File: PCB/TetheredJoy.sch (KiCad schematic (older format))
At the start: 9 parts

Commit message: worked on schematic
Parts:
- added D? (x4): LED, symbol Device:LED
- added R? (x5): 470, symbol Device:R_Small
- added R? (x5): 47K, symbol Device:R_Small
- added SW? (x4): SW_Push, symbol Switch:SW_Push
- R?: value R_Small -> 470
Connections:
- net +5V: now also C?.1, C?.1, J?.2 (Pin_2), U?.14 (VDD), R?.1, R?.1, R?.1, R?.1, R?.1, R?.1, R?.1, R?.1, R?.1
- net GND: now also C?.2, J?.3 (Pin_3), U?.5 (VSS), SW?.2, SW?.2, SW?.2, SW?.2
- net at U?.1 (Vref/AN2/RA2): now also J?.5 (Pin_5), R?.2
- net LED4SW4: now reaches U?.10 (RB4/PGM)
- net LED4SW4: now also D?.1 (K), R?.2, SW?.1
- net TX: now reaches U?.11 (RB5)
- net TX: now also J?.4 (Pin_4)
- net PGC: now reaches U?.12 (RB6/T1OSC0/T1CKI/PGC)
- net PGC: now also J?.5 (Pin_5)
- net PGD: now reaches U?.13 (RB7/T1OSI/PGD)
- net PGD: now also J?.4 (Pin_4)
- net at U?.15 (CLKOUT/OSC2/RA6): now also D?.2 (AK)
- net at U?.16 (CLKIN/OSC1/RA7): now also R?.1
- net at U?.2 (CMP1/AN3/RA3): now also D?.2 (AK)
- net at U?.3 (TOCKI/CMP2/RA4): now also R?.1
- net Vpp: now reaches U?.4 (~MCLR~/Vpp/RA5)
- net Vpp: now also J?.1 (Pin_1)
- net LED1SW1: now reaches U?.6 (RB0/INT)
- net LED1SW1: now also D?.1 (K), R?.2, SW?.1
- net LED2SW2: now reaches U?.7 (RB1/RX/DT)
- net LED2SW2: now also D?.1 (K), R?.2, SW?.1
- net RX: now reaches U?.8 (RB2/TX/CK)
- net RX: now also J?.3 (Pin_3)
- net LED3SW3: now reaches U?.9 (RB3/CCP1)
- net LED3SW3: now also D?.1 (K), R?.2, SW?.1
- net at D?.1 (KA): now also R?.2 (x2)
- new net: D?.2 (A), R?.2 (x4)
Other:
- moved on the sheet: C?, R?

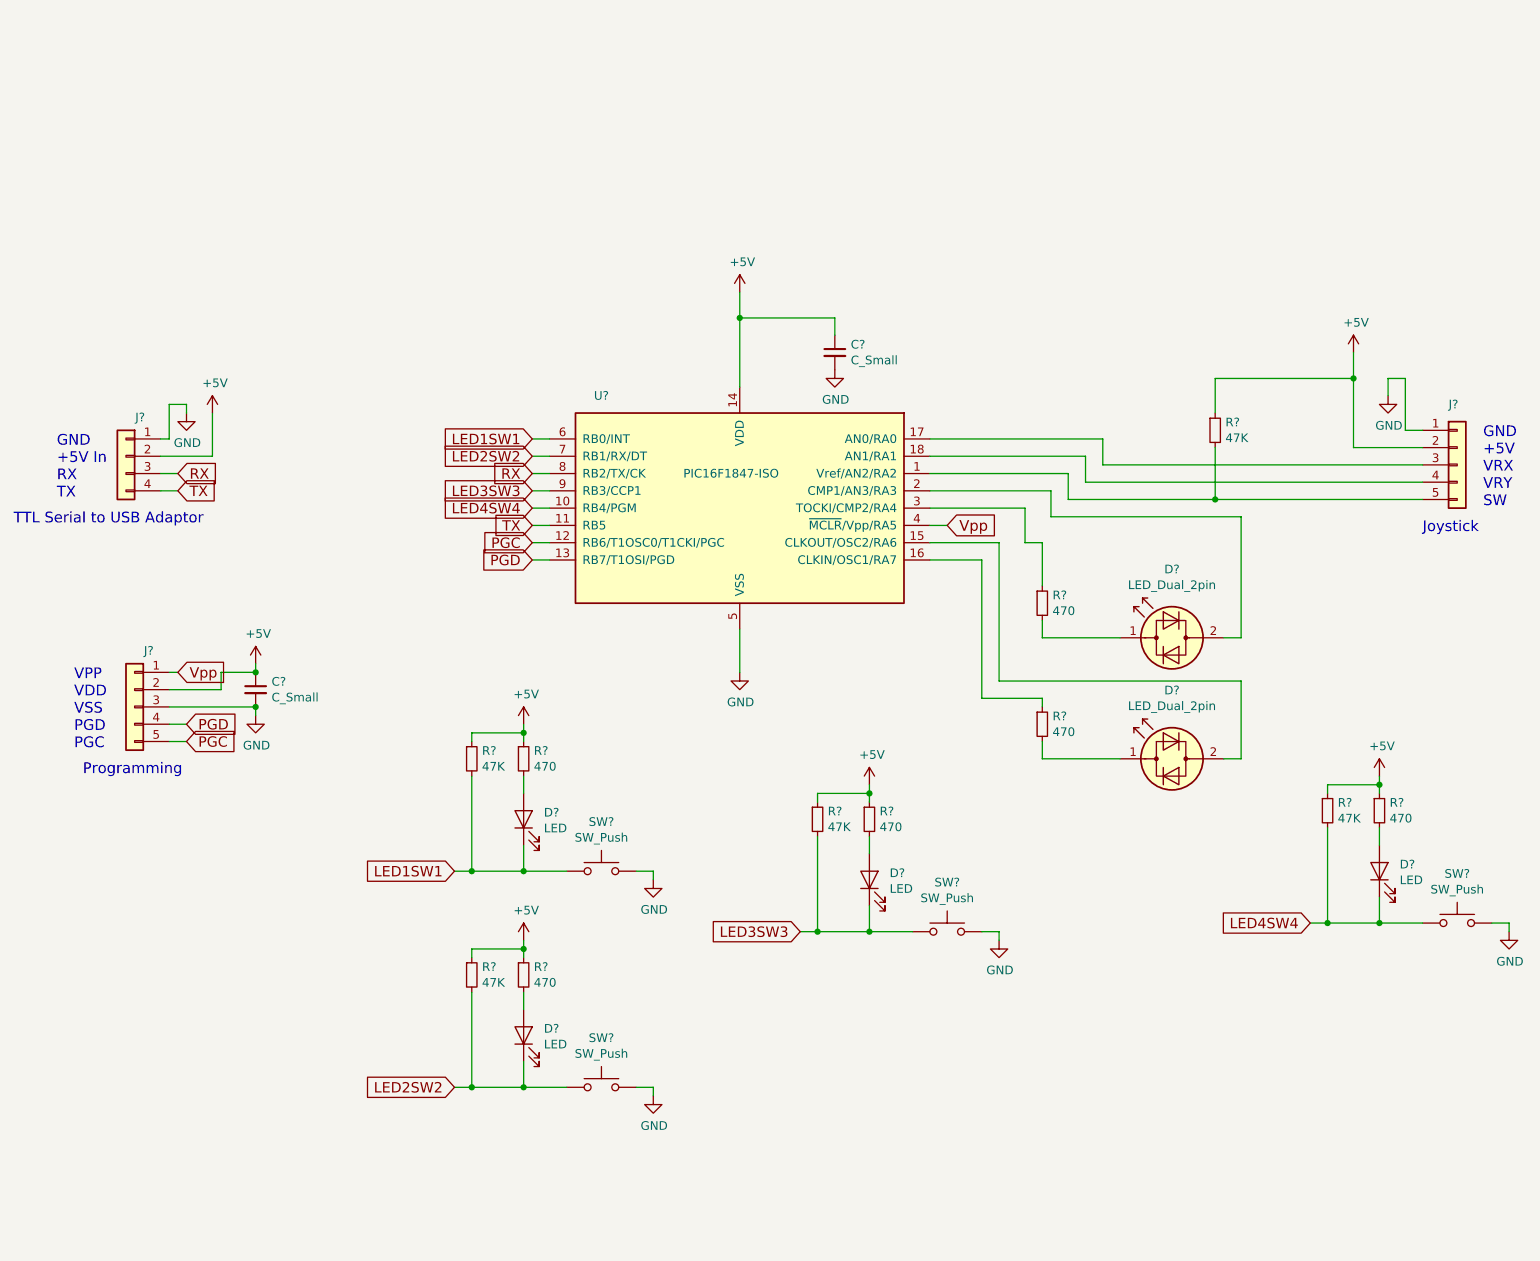
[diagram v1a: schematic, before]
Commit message: Schematic done
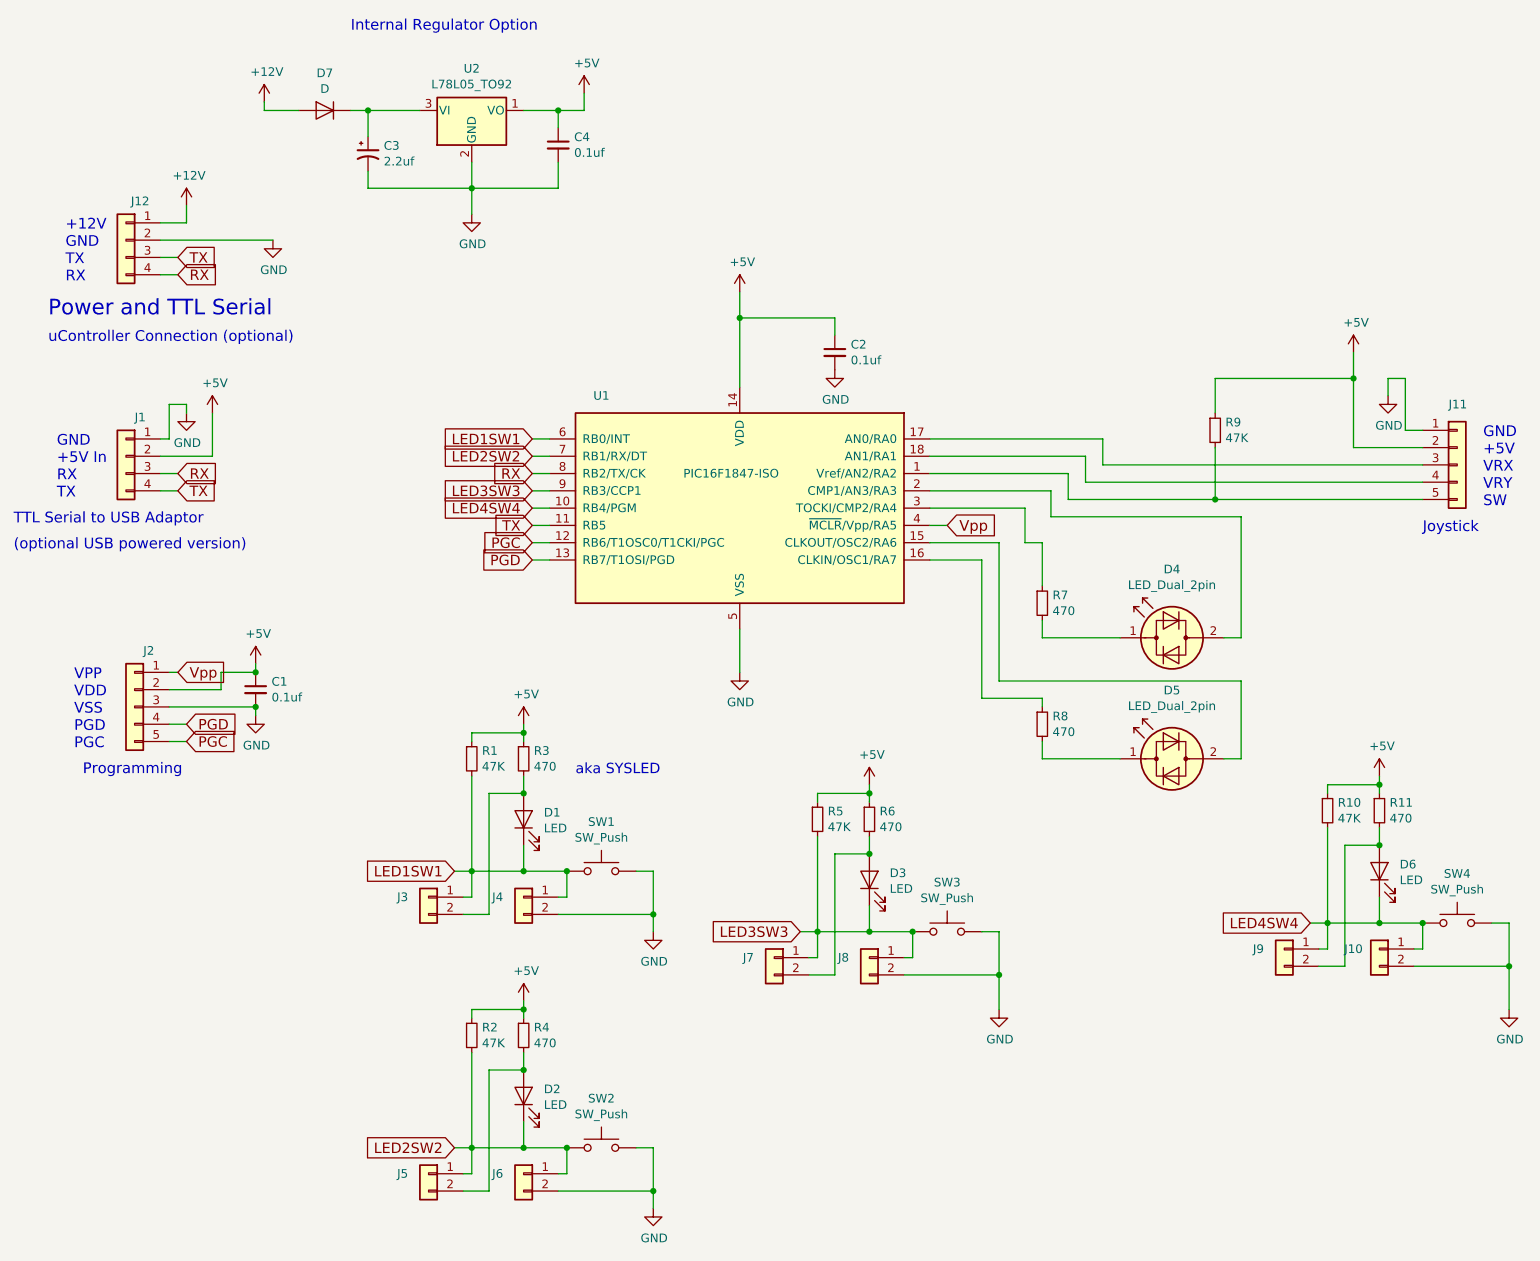
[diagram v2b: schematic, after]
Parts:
- added C3: 2.2uf, Capacitor_THT:CP_Radial_D4.0mm_P2.00mm, symbol Device:CP1_Small
- added C4: 0.1uf, Capacitor_SMD:C_0805_2012Metric_Pad1.15x1.40mm_HandSolder, symbol Device:C_Small
- added D7: D, Diode_SMD:D_SMA_Handsoldering, symbol Device:D
- added J10, J3, J4, J5, J6, J7, J8, J9: Conn_01x02, Connector_PinHeader_2.54mm:PinHeader_1x02_P2.54mm_Vertical, symbol Connector_Generic:Conn_01x02
- added J12: Conn_01x04, Connector_PinHeader_2.54mm:PinHeader_1x04_P2.54mm_Vertical, symbol Connector_Generic:Conn_01x04
- added U2: L78L05_TO92, Package_TO_SOT_THT:TO-92_Inline, symbol Regulator_Linear:L78L05_TO92
- C1, C2: renamed from C?; value C_Small -> 0.1uf; footprint (none) -> Capacitor_SMD:C_0805_2012Metric_Pad1.15x1.40mm_HandSolder
- D1, D2, D3: renamed from D?; footprint (none) -> LED_SMD:LED_1206_3216Metric_Pad1.42x1.75mm_HandSolder
- D4, D5, D6: renamed from D?; footprint (none) -> LED_SMD:LED_0805_2012Metric_Pad1.15x1.40mm_HandSolder
- J1: renamed from J?; footprint (none) -> Connector_PinHeader_2.54mm:PinHeader_1x04_P2.54mm_Vertical
- J11, J2: renamed from J?; footprint (none) -> Connector_PinHeader_2.54mm:PinHeader_1x05_P2.54mm_Vertical
- R1, R10, R11, R2, R3, R4, R5, R6, R7, R8, R9: renamed from R?; footprint (none) -> Resistor_SMD:R_0805_2012Metric_Pad1.15x1.40mm_HandSolder
- SW1, SW2, SW3, SW4: renamed from SW?; footprint (none) -> Button_Switch_SMD:SW_SPST_PTS645
- U1: renamed from U?; footprint (none) -> Package_SO:SOIC-18W_7.5x11.6mm_P1.27mm
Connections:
- net +5V: now also C4.1, U2.1 (VO)
- net GND: now also C3.2, C4.2, J10.2 (Pin_2), J12.2 (Pin_2), J4.2 (Pin_2), J6.2 (Pin_2), J8.2 (Pin_2), U2.2 (GND)
- net LED1SW1: now also J3.1 (Pin_1), J4.1 (Pin_1)
- net LED2SW2: now also J5.1 (Pin_1), J6.1 (Pin_1)
- net LED3SW3: now also J7.1 (Pin_1), J8.1 (Pin_1)
- net LED4SW4: now also J10.1 (Pin_1), J9.1 (Pin_1)
- net RX: now also J12.4 (Pin_4)
- net TX: now also J12.3 (Pin_3)
- net at D1.2 (A), R3.2: now also J3.2 (Pin_2)
- net at D2.2 (A), R4.2: now also J5.2 (Pin_2)
- net at D3.2 (A), R6.2: now also J7.2 (Pin_2)
- net at D6.2 (A), R11.2: now also J9.2 (Pin_2)
- new net: C3.1, D7.1 (K), U2.3 (VI)
- new net +12V: D7.2 (A), J12.1 (Pin_1)
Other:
- note added: "(optional USB powered version)"
- note added: "+12V\nGND\nTX\nRX"
- note added: "Internal Regulator Option"
- note added: "Power and TTL Serial"
- note added: "aka SYSLED"
- note added: "uController Connection (optional)"
- moved on the sheet: D2, R2, R4, SW2

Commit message: PCB done
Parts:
- D4, D5, D6: footprint LED_SMD:LED_0805_2012Metric_Pad1.15x1.40mm_HandSolder -> LED_SMD:LED_1206_3216Metric_Pad1.42x1.75mm_HandSolder
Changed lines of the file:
@@
 F 0 "D4" H 7250 4696 50  0000 C CNN
 F 1 "LED_Dual_2pin" H 7250 4605 50  0000 C CNN
-F 2 "LED_SMD:LED_0805_2012Metric_Pad1.15x1.40mm_HandSolder" H 7250 4300 50  0001 C CNN
+F 2 "LED_SMD:LED_1206_3216Metric_Pad1.42x1.75mm_HandSolder" H 7250 4300 50  0001 C CNN
 F 3 "~" H 7250 4300 50  0001 C CNN
 	1    7250 4300
@@
 F 0 "D5" H 7250 5396 50  0000 C CNN
 F 1 "LED_Dual_2pin" H 7250 5305 50  0000 C CNN
-F 2 "LED_SMD:LED_0805_2012Metric_Pad1.15x1.40mm_HandSolder" H 7250 5000 50  0001 C CNN
+F 2 "LED_SMD:LED_1206_3216Metric_Pad1.42x1.75mm_HandSolder" H 7250 5000 50  0001 C CNN
 F 3 "~" H 7250 5000 50  0001 C CNN
 	1    7250 5000
@@
 F 0 "D6" V 8489 5533 50  0000 R CNN
 F 1 "LED" V 8398 5533 50  0000 R CNN
-F 2 "LED_SMD:LED_0805_2012Metric_Pad1.15x1.40mm_HandSolder" H 8450 5650 50  0001 C CNN
+F 2 "LED_SMD:LED_1206_3216Metric_Pad1.42x1.75mm_HandSolder" H 8450 5650 50  0001 C CNN
 F 3 "~" H 8450 5650 50  0001 C CNN
 	1    8450 5650
